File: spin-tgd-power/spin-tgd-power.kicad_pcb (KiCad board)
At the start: 2 copper layers, 52 x 19 mm, 20 parts, among them J1 FT_switch, J10 Conn_01x01, J11 Conn_01x01, J2 bat_high, J3 bat_low, J4 Conn_01x01, J5 Conn_01x01, J6 Conn_01x01, J7 Conn_01x01, J8 ESC_Foo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

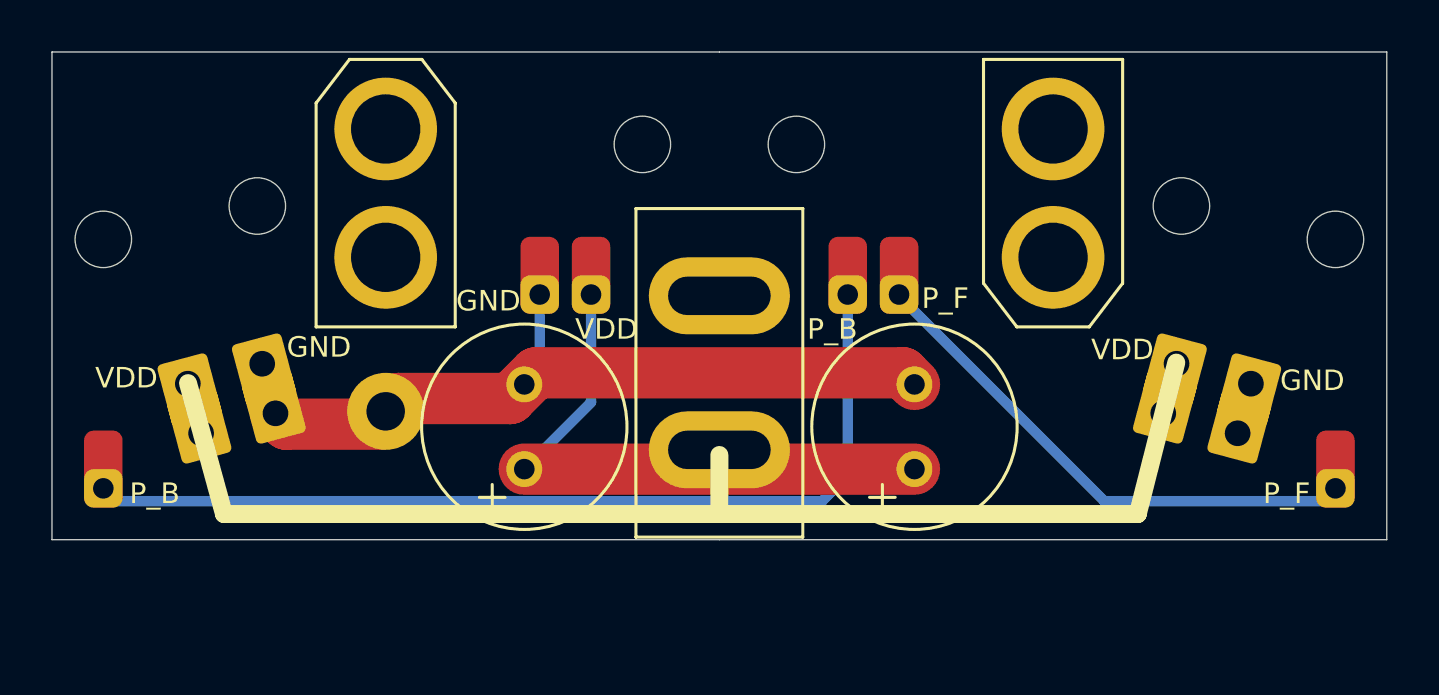
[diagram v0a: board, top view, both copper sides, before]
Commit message: DSP DAC circuit and FO card todo notes
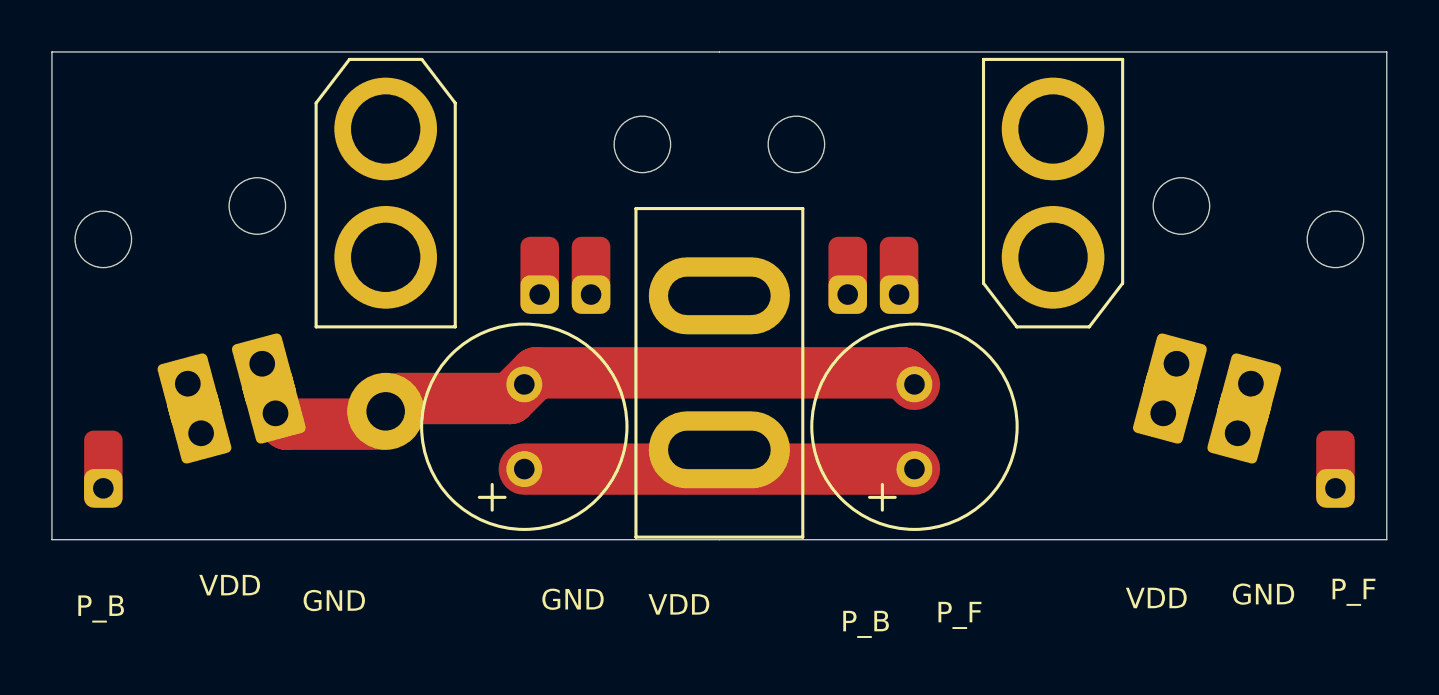
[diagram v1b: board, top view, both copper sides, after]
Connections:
- J8 pad 1: VDD -> GND
- J8 pad 2: GND -> VDD
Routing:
- net PPM_B: track 35.9 -> 0.00 mm
- net PPM_F: track 20.6 -> 0.00 mm
- net VDD: track 22.3 -> 15.2 mm
- net GND: track 28.6 -> 25.7 mm
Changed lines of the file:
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@@
     (fp_rect (start 2.75 2.218) (end -2.75 -2.282) (layer "F.CrtYd") (width 0.05) (fill none))
     (pad "1" thru_hole roundrect (at -1.5 1 165) (size 2 2.5) (drill 1 (offset 0 0.25)) (layers *.Cu *.Mask) (roundrect_rratio 0.1)
-      (net 4 "VDD") (pinfunction "Pin_1") (pintype "passive"))
+      (net 1 "GND") (pinfunction "Pin_1") (pintype "passive"))
     (pad "1" thru_hole roundrect (at -1.5 -1 345) (size 2 2.5) (drill 1 (offset 0 0.25)) (layers *.Cu *.Mask) (roundrect_rratio 0.1)
-      (net 4 "VDD") (pinfunction "Pin_1") (pintype "passive"))
+      (net 1 "GND") (pinfunction "Pin_1") (pintype "passive"))
     (pad "2" thru_hole roundrect (at 1.5 -1 345) (size 2 2.5) (drill 1 (offset 0 0.25)) (layers *.Cu *.Mask) (roundrect_rratio 0.1)
-      (net 1 "GND") (pinfunction "Pin_2") (pintype "passive"))
+      (net 4 "VDD") (pinfunction "Pin_2") (pintype "passive"))
     (pad "2" thru_hole roundrect (at 1.5 1 165) (size 2 2.5) (drill 1 (offset 0 0.25)) (layers *.Cu *.Mask) (roundrect_rratio 0.1)
-      (net 1 "GND") (pinfunction "Pin_2") (pintype "passive"))
+      (net 4 "VDD") (pinfunction "Pin_2") (pintype "passive"))
   )
   (footprint "" (layer "F.Cu")
@@
       (pinfunction "Pin_2") (pintype "passive"))
   )
-  (gr_line (start 2.75 8) (end 13 8) (layer "B.SilkS") (width 0.7))
-  (gr_line (start 13 1.7) (end -12.9 1.7) (layer "B.SilkS") (width 0.7))
-  (gr_line (start 1.3 9.5) (end 2.75 8) (layer "B.SilkS") (width 0.7))
-  (gr_line (start -13 14) (end -13 7.9) (layer "B.SilkS") (width 0.7))
-  (gr_line (start 16.3 18) (end 17.8 12.1) (layer "F.SilkS") (width 0.7))
-  (gr_line (start 0 18) (end -19.3 18) (layer "F.SilkS") (width 0.7))
-  (gr_line (start 0 18) (end 0 15.7) (layer "F.SilkS") (width 0.7))
-  (gr_line (start 0 18) (end 16.3 18) (layer "F.SilkS") (width 0.7))
-  (gr_line (start -19.3 18) (end -20.7 12.9) (layer "F.SilkS") (width 0.7))
   (gr_line (start -13 14.5) (end -16.9 14.5) (layer "F.Mask") (width 2))
   (gr_line (start -26 0) (end -26 19) (layer "Edge.Cuts") (width 0.05))
@@
     (effects (font (size 0.8 0.8) (thickness 0.2)) (justify mirror))
   )
-  (gr_text "VDD\n" (at 15.7 11.6) (layer "F.SilkS")
-    (effects (font (size 0.8 0.8) (thickness 0.2)))
-  )
-  (gr_text "VDD\n" (at -23.1 12.7) (layer "F.SilkS")
-    (effects (font (size 0.8 0.8) (thickness 0.2)))
-  )
-  (gr_text "GND" (at -15.6 11.5) (layer "F.SilkS")
-    (effects (font (size 0.8 0.8) (thickness 0.2)))
-  )
-  (gr_text "P_F\n" (at 8.8 9.6) (layer "F.SilkS")
-    (effects (font (size 0.8 0.8) (thickness 0.2)))
-  )
-  (gr_text "GND" (at -9 9.7) (layer "F.SilkS")
-    (effects (font (size 0.8 0.8) (thickness 0.2)))
-  )
-  (gr_text "VDD\n" (at -4.4 10.8) (layer "F.SilkS")
-    (effects (font (size 0.8 0.8) (thickness 0.2)))
-  )
-  (gr_text "P_B" (at 4.4 10.8) (layer "F.SilkS")
-    (effects (font (size 0.8 0.8) (thickness 0.2)))
-  )
-  (gr_text "P_F\n" (at 22.1 17.2) (layer "F.SilkS")
-    (effects (font (size 0.8 0.8) (thickness 0.2)))
-  )
-  (gr_text "P_B" (at -22 17.2) (layer "F.SilkS")
-    (effects (font (size 0.8 0.8) (thickness 0.2)))
-  )
-  (gr_text "GND" (at 23.1 12.8) (layer "F.SilkS")
+  (gr_text "VDD\n" (at 17.05 21.3) (layer "F.SilkS")
+    (effects (font (size 0.8 0.8) (thickness 0.2)))
+  )
+  (gr_text "VDD\n" (at -19.05 20.8) (layer "F.SilkS")
+    (effects (font (size 0.8 0.8) (thickness 0.2)))
+  )
+  (gr_text "GND" (at -15 21.4) (layer "F.SilkS")
+    (effects (font (size 0.8 0.8) (thickness 0.2)))
+  )
+  (gr_text "P_F\n" (at 9.35 21.85) (layer "F.SilkS")
+    (effects (font (size 0.8 0.8) (thickness 0.2)))
+  )
+  (gr_text "GND" (at -5.7 21.35) (layer "F.SilkS")
+    (effects (font (size 0.8 0.8) (thickness 0.2)))
+  )
+  (gr_text "VDD\n" (at -1.55 21.55) (layer "F.SilkS")
+    (effects (font (size 0.8 0.8) (thickness 0.2)))
+  )
+  (gr_text "P_B" (at 5.7 22.2) (layer "F.SilkS")
+    (effects (font (size 0.8 0.8) (thickness 0.2)))
+  )
+  (gr_text "P_F\n" (at 24.7 20.95) (layer "F.SilkS")
+    (effects (font (size 0.8 0.8) (thickness 0.2)))
+  )
+  (gr_text "P_B" (at -24.1 21.6) (layer "F.SilkS")
+    (effects (font (size 0.8 0.8) (thickness 0.2)))
+  )
+  (gr_text "GND" (at 21.2 21.15) (layer "F.SilkS")
     (effects (font (size 0.8 0.8) (thickness 0.2)))
   )
@@
   (segment (start -7.15 12.5) (end -8.15 13.5) (width 2) (layer "F.Cu") (net 1))
   (segment (start 7.15 12.5) (end -7.15 12.5) (width 2) (layer "F.Cu") (net 1))
-  (segment (start -7 12.35) (end -7.6 12.95) (width 0.4064) (layer "B.Cu") (net 1))
-  (segment (start -7 10.25) (end -7 12.35) (width 0.4064) (layer "B.Cu") (net 1))
   (segment (start -7.6 16.25) (end 7.6 16.25) (width 2) (layer "F.Cu") (net 4))
-  (segment (start -5 10.25) (end -5 13.65) (width 0.4064) (layer "B.Cu") (net 4))
-  (segment (start -5 13.65) (end -7.6 16.25) (width 0.4064) (layer "B.Cu") (net 4))
-  (segment (start 23.5 17.5) (end 24 17) (width 0.4064) (layer "B.Cu") (net 5))
-  (segment (start 15 17.5) (end 23.5 17.5) (width 0.4064) (layer "B.Cu") (net 5))
-  (segment (start 7 9.5) (end 15 17.5) (width 0.4064) (layer "B.Cu") (net 5))
-  (segment (start 7 9.45) (end 7 9.5) (width 0.4064) (layer "B.Cu") (net 5))
-  (segment (start -23.5 17.5) (end -24 17) (width 0.4064) (layer "B.Cu") (net 6))
-  (segment (start 5 16.5) (end 4 17.5) (width 0.4064) (layer "B.Cu") (net 6))
-  (segment (start 5 10.25) (end 5 16.5) (width 0.4064) (layer "B.Cu") (net 6))
-  (segment (start 4 17.5) (end -23.5 17.5) (width 0.4064) (layer "B.Cu") (net 6))
 )

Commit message: Eggman V2 ordered gerbers
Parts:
- removed the ? at (3.00, 3.60)
- removed the ? at (-3.00, 3.60)
- removed J10, J11, J7: Conn_01x01, lib_fp:TGD-antenna-THT
- added C3: 4.7nF, Capacitor_SMD:C_0603_1608Metric, F.Cu at (-5.80, 6.25)
- added D1: ZMM3V3, Diode_SMD:D_MiniMELF, F.Cu at (7.40, 8.00)
- added R1: 5mR, Resistor_SMD:R_2512_6332Metric_Pad1.40x3.35mm_HandSolder, B.Cu at (-13.0, 10.2)
- added R2: 100R, Resistor_SMD:R_0603_1608Metric, F.Cu at (-5.80, 7.90)
- added R3: 1K, Resistor_SMD:R_0603_1608Metric, F.Cu at (5.10, 8.10)
- added U1: INA185A1, Package_TO_SOT_SMD:SOT-563, F.Cu at (-7.40, 9.90)
- J2, J3: footprint lib_fp:TGD_AMASS_XT30U-F_1x02_P5.0mm_Vertical -> AlfredoFootprints:TGD_2P_BatHoles
- J4: value Conn_01x01 -> Conn_01x05; footprint lib_fp:TGD-antenna-THT -> Connector_JST:JST_EH_B5B-EH-A_1x05_P2.50mm_Vertical
- J5, J6: footprint lib_fp:TGD-antenna-THT -> AlfredoFootprints:TGD-antenna-THT
- moved J5 30.0 mm to (-24.0, 16.2)
- moved J6 30.0 mm to (24.0, 16.2)
- moved J4 13.5 mm to (-5.00, 2.50)
- moved C1 3.82 mm to (-3.80, 15.0)
- moved C2 3.82 mm to (3.80, 15.0)
- moved J2 1.75 mm to (13.0, 3.75)
- moved J3 1.75 mm to (-13.0, 3.75)
- moved ? 1.00 mm to (-13.0, 15.0)
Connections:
- ? pad 2: GND -> /sns+
- C1 pad 2: GND -> /sns+
- C2 pad 2: GND -> /sns+
- J4 pad 1: PPM_F -> CurSns
- J6 pad 1: VDD -> PPM_F
- J8 pad 1: GND -> /sns+
- J9 pad 2: GND -> /sns+
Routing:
- net /sns+: track 0.00 -> 41.3 mm
- net PPM_B: track 0.00 -> 35.8 mm
- net PPM_F: track 0.00 -> 28.2 mm
- net VDD: track 15.2 -> 37.4 mm
- net GND: track 25.7 -> 43.5 mm
- net +3V3: track 0.00 -> 15.9 mm
- net CurSns: track 0.00 -> 5.43 mm
- net Net-(R2-Pad2): track 0.00 -> 2.08 mm
- added copper zone on B.Cu, net /sns+
- added copper zone on B.Cu, net GND
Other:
- outline, holes or cut-outs redrawn
- board text added: "CrS"
- board text added: "SPIN-TGD-EGGMAN V3"
- board text removed: "SPIN-TGD-EGGMAN V2"
